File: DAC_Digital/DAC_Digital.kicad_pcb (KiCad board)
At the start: 2 copper layers, 100 x 100 mm, 131 parts, among them J1 +5V_in, J10 USB_Dev4, J11 P9, J12 Anlg_in, J13 Anlg_I2C, J14 P8, J15 Test, J16 Test, J17 Fix, J18 Fix, J19 Fix, J2 DBG_PORT, J20 Fix, J3 DSPL_PORT, J4 Out_SPDIF, J5 USB0, J6 USB1, J7 USB_Dev1, J8 USB_Dev2, J9 USB_Dev3, Q1 2n7002, Q2 2N7002, Q3 FDS4435, Q4 FDS4435, Q5 2N7002, Q6 2N7002, T1 DA103C, U1 CS8406_2, U2 PIC18F6722, U3 74LVC1G08GW, U4 PCM2903C, U5 74LVC1G08GW, U6 USB2514B-AEZC, U7 NE5532, X1 7A-24.000MAAJ-T, Y1 10MHz, Y2 12MHz

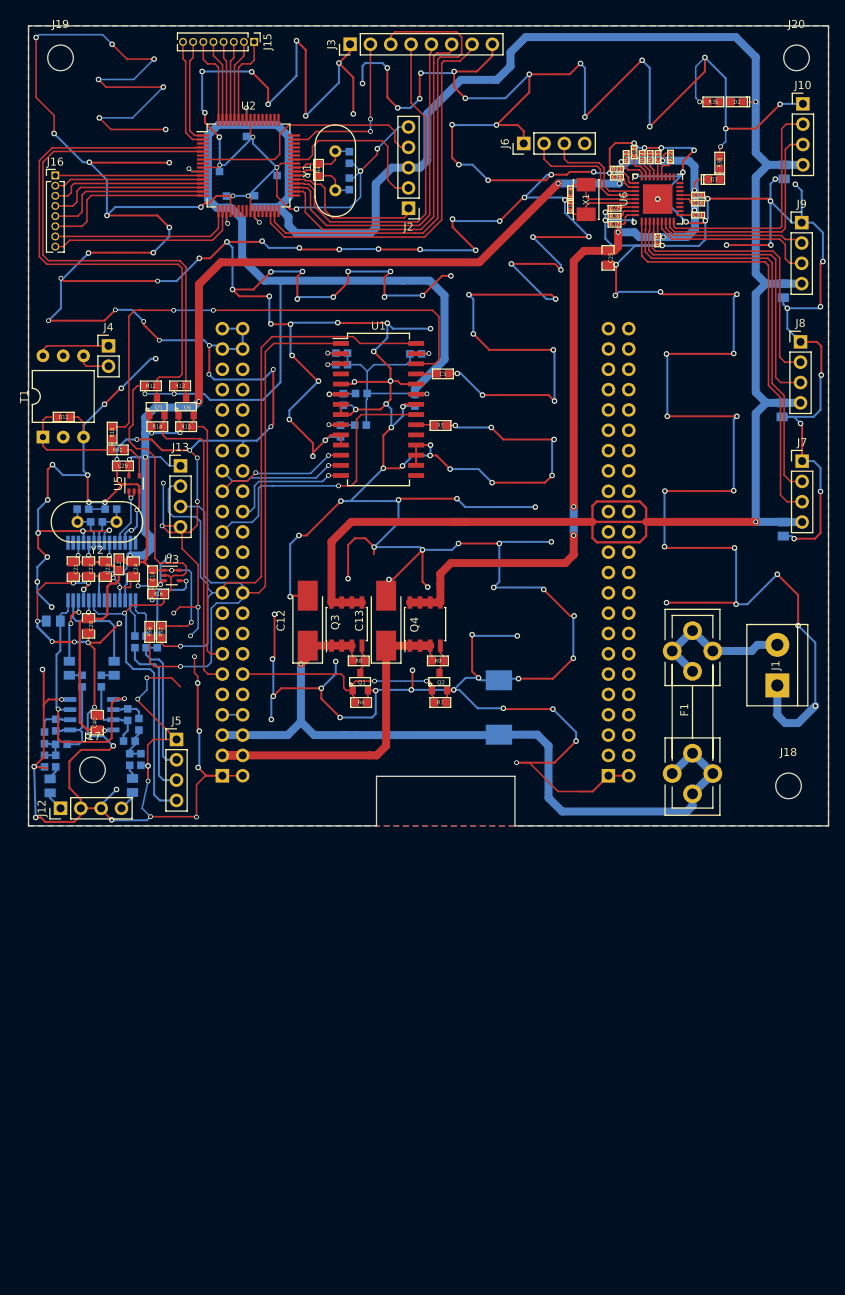
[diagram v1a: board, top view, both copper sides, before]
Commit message: Update DAC digital board, switch to odroid C2
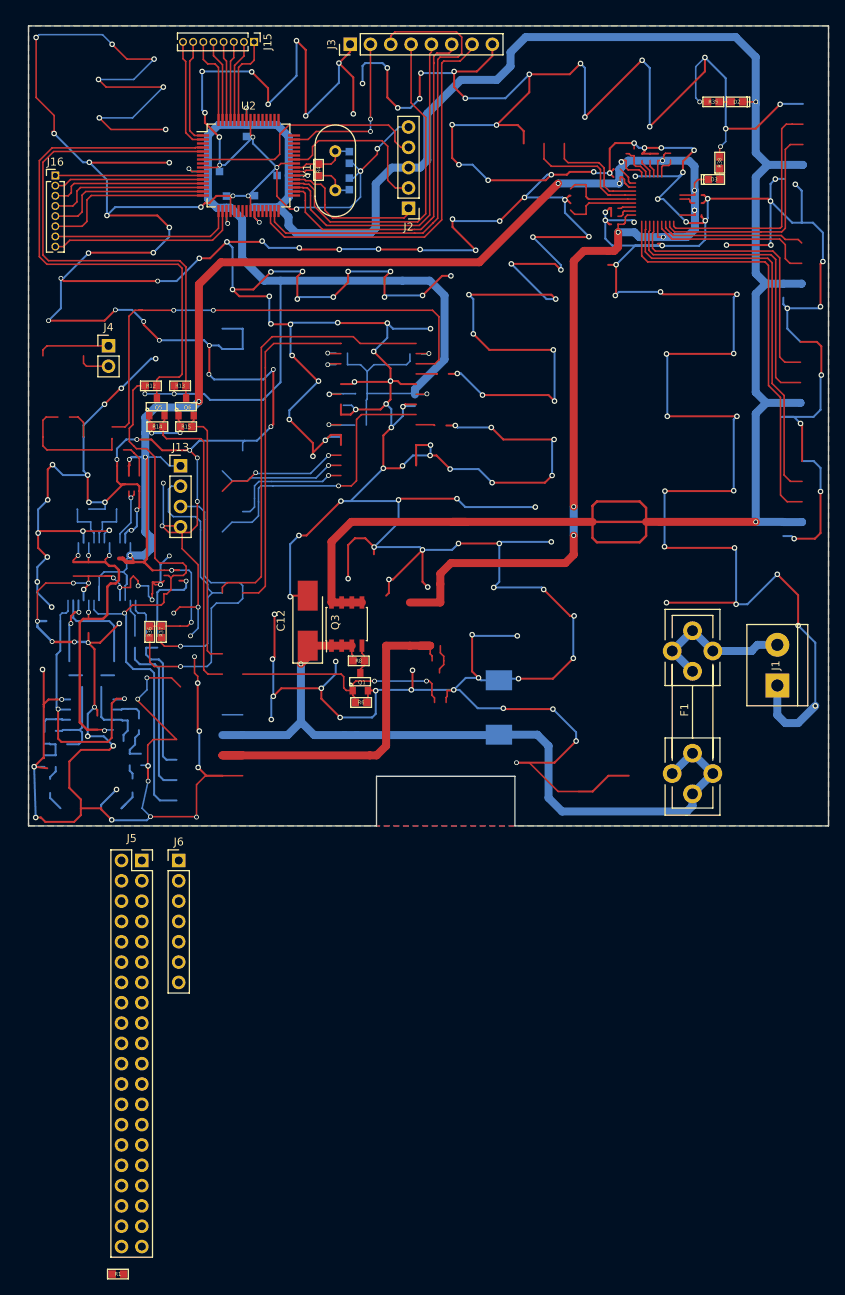
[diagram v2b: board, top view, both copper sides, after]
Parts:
- removed C1, C14, C2, C29, C3, C5: 100n, Yame_library:SM0603-MR
- removed C13: 100u, Capacitors_Tantalum_SMD:CP_Tantalum_Case-U_EIA-6032-15_Hand
- removed C15, C16: 18p, Yame_library:SM0603-MR
- removed C17, C19: 18p, Yame_library:SM0402-MR
- removed C18, C27, C28, C30, C31, C32, C35, C36, C37: 100n, Yame_library:SM0402-MR
- removed C20, C21, C22, C23, C24, C25, C26, C33, C34, C40, C43, C44, C45, C46, C47, C48: 10u, Yame_library:SM0805-MR
- removed C38, C39, C41, C42: 330p, Yame_library:SM0603-MR
- removed J10: USB_Dev4, Pin_Headers:Pin_Header_Straight_1x04_Pitch2.54mm
- removed J11: P9, Pin_Headers:Pin_Header_Straight_2x23_Pitch2.54mm
- removed J12: Anlg_in, Pin_Headers:Pin_Header_Straight_1x04_Pitch2.54mm
- removed J14: P8, Pin_Headers:Pin_Header_Straight_2x23_Pitch2.54mm
- removed J17, J18, J19, J20: Fix, Mounting_Holes:MountingHole_3.2mm_M3
- removed J7: USB_Dev1, Pin_Headers:Pin_Header_Straight_1x04_Pitch2.54mm
- removed J8: USB_Dev2, Pin_Headers:Pin_Header_Straight_1x04_Pitch2.54mm
- removed J9: USB_Dev3, Pin_Headers:Pin_Header_Straight_1x04_Pitch2.54mm
- removed L1, L2: BLM18AG102SN1D, Yame_library:SM0603-MR
- removed Q2: 2N7002, Yame_library:SOT23-MR
- removed Q4: FDS4435, Housings_SOIC:SOIC-8_3.9x4.9mm_Pitch1.27mm
- removed R10, R40: 390, Yame_library:SM0603-MR
- removed R11: 91, Yame_library:SM0603-MR
- removed R16, R17: 1M, Yame_library:SM0603-MR
- removed R18: 1,5k, Yame_library:SM0603-MR
- removed R19, R20: 22, Yame_library:SM0603-MR
- removed R2, R3: R, Yame_library:SM0603-MR
- removed R21, R22, R23, R24, R25: 47k, Yame_library:SM0402-MR
- removed R26: 12k, Yame_library:SM0402-MR
- removed R27, R28: 100, Yame_library:SM0603-MR
- removed R29, R30, R33, R34: 12k, Yame_library:SM0603-MR
- removed R31, R32: 3.9k, Yame_library:SM0603-MR
- removed R39, R7, R9: 1meg, Yame_library:SM0603-MR
- removed R5: 47k, Yame_library:SM0603-MR
- removed T1: DA103C, Housings_DIP:DIP-6_W10.16mm
- removed U1: CS8406_2, Housings_SOIC:SOIC-28W_7.5x18.7mm_Pitch1.27mm
- removed U3, U5: 74LVC1G08GW, TO_SOT_Packages_SMD:SOT-353_SC-70-5
- removed U4: PCM2903C, Housings_SSOP:SSOP-28_5.3x10.2mm_Pitch0.65mm
- removed U6: USB2514B-AEZC, Housings_DFN_QFN:QFN-36-1EP_6x6mm_Pitch0.5mm
- removed U7: NE5532, Housings_SOIC:SOIC-8_3.9x4.9mm_Pitch1.27mm
- removed X1: 7A-24.000MAAJ-T, Yame_library:7A_SERIES_TXC
- removed Y2: 12MHz, Crystals:Crystal_HC49-4H_Vertical
- J5: value USB0 -> Conn_02x20_Odd_Even; footprint Pin_Headers:Pin_Header_Straight_1x04_Pitch2.54mm -> Connector_PinSocket_2.54mm:PinSocket_2x20_P2.54mm_Vertical
- J6: value USB1 -> Conn_01x07; footprint Pin_Headers:Pin_Header_Straight_1x04_Pitch2.54mm -> Connector_PinHeader_2.54mm:PinHeader_1x07_P2.54mm_Vertical
- R1: value R -> 10k; moved to F.Cu
- moved R1 118.5 mm to (33.2, 244.0)
- moved J6 99.5 mm to (40.8, 192.3), turned to 0 degrees
- moved J5 15.7 mm to (36.2, 192.3)
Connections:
- net /VDD_5V_USB1 renamed Net-(J6-Pad4)
- net Net-(J3-Pad2) renamed /IntIR
- net Net-(J3-Pad3) renamed /IntB
- net Net-(J3-Pad4) renamed /MOSI
- net Net-(J3-Pad5) renamed /MISO
- net Net-(J3-Pad6) renamed /SCK
- net Net-(J3-Pad7) renamed //CS
- net VCC renamed /+3.3v_Dev
- C10 pad 2: GND -> GNDD
- C11 pad 2: GND -> GNDD
- C12 pad 2: GND -> GNDD
- C4 pad 2: GND -> GNDD
- C6 pad 2: GND -> GNDD
- C7 pad 2: GND -> GNDD
- C8 pad 2: GND -> GNDD
- C9 pad 2: GND -> GNDD
- D1 pad 2: GND -> GNDD
- J1 pad 1: GND -> GNDD
- J13 pad 4: GND -> GNDD
- J2 pad 3: /+5v_Dev -> /VDD_5V
- J2 pad 5: GND -> GNDD
- J3 pad 1: GND -> GNDD
- J3 pad 8: GND -> GNDD
- J5 pad 1: GND -> Net-(J5-Pad1)
- J5 pad 4: /+5v_Dev -> Net-(J5-Pad4)
- J6 pad 1: GND -> Net-(J6-Pad1)
- Q1 pad 2: GND -> GNDD
- R1 pad 1: Net-(R1-Pad1) -> /VDD_5V
- R1 pad 2: /+5v_Dev -> Net-(J2-Pad4)
- R12 pad 1: /+5v_Dev -> /VDD_5V
- R13 pad 1: /+5v_Dev -> /VDD_5V
- R35 pad 2: GND -> GNDD
- R38 pad 2: GND -> GNDD
- R6 pad 2: GND -> GNDD
- U2 pad 10: /+5v_Dev -> /VDD_5V
- U2 pad 19: /+5v_Dev -> /VDD_5V
- U2 pad 20: GND -> GNDD
- U2 pad 25: GND -> GNDD
- U2 pad 26: /+5v_Dev -> /VDD_5V
- U2 pad 38: /+5v_Dev -> /VDD_5V
- U2 pad 41: GND -> GNDD
- U2 pad 56: GND -> GNDD
- U2 pad 57: /+5v_Dev -> /VDD_5V
- U2 pad 9: GND -> GNDD
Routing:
- net GNDD: track 0.00 -> 1745.5 mm, vias 0 -> 266
- net GND: track 1745.5 -> 0.00 mm, vias 266 -> 0
- added copper zone on B.Cu, net GNDD
- added copper zone on F.Cu, net GNDD
- removed copper zone on B.Cu, net GND
- removed copper zone on F.Cu, net GND
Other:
- board text added: "1"
- board text added: "2"
- board text added: "23.5mm"
- board text added: "39"
- board text added: "40"
- board text added: "49.00mm"
- board text added: "56mm"
- board text added: "58mm"
- board text added: "5V DCJACK"
- board text added: "85mm"
- board text added: "ALIVE"
- board text added: "C10"
- board text added: "C100"
- board text added: "C101A"
- board text added: "C101B"
- board text added: "C102A"
- board text added: "C102B"
- board text added: "C103A"
- board text added: "C103B"
- board text added: "C104"
- board text added: "C105"
- board text added: "C106"
- board text added: "C107"
- board text added: "C108"
- board text added: "C109"
- board text added: "C11"
- board text added: "C112"
- board text added: "C113"
- board text added: "C114"
- board text added: "C12"
- board text added: "C124"
- board text added: "C136"
- board text added: "C14"
- board text added: "C15"
- board text added: "C159"
- board text added: "C160"
- board text added: "C164"
- board text added: "C22"
- board text added: "C23"
- board text added: "C25"
- board text added: "C27"
- board text added: "C28"
- board text added: "C29"
- board text added: "C3"
- board text added: "C30"
- board text added: "C38"
- board text added: "C4"
- board text added: "C40"
- board text added: "C42"
- board text added: "C43"
- board text added: "C44"
- board text added: "C45"
- board text added: "C46"
- board text added: "C48"
- board text added: "C52"
- board text added: "C57"
- board text added: "C58"
- board text added: "C59"
- board text added: "C6"
- board text added: "C60"
- board text added: "C61"
- board text added: "C62"
- board text added: "C63"
- board text added: "C64"
- board text added: "C65"
- board text added: "C66"
- board text added: "C67"
- board text added: "C68"
- board text added: "C69"
- board text added: "C7"
- board text added: "C71"
- board text added: "C72"
- board text added: "C75"
- board text added: "C76"
- board text added: "C77"
- board text added: "C78"
- board text added: "C79"
- board text added: "C8"
- board text added: "C82"
- board text added: "C83"
- board text added: "C84"
- board text added: "C86"
- board text added: "C87"
- board text added: "C88"
- board text added: "C89"
- board text added: "C90"
- board text added: "C91"
- board text added: "C92"
- board text added: "C95"
- board text added: "C96"
- board text added: "C97"
- board text added: "C98"
- board text added: "C99"
- board text added: "CON2"
- board text added: "CON3"
- board text added: "CON5"
- board text added: "CON6A"
- board text added: "CON6B"
- board text added: "CVBS"
- board text added: "D1"
- board text added: "D2"
- board text added: "FB1"
- board text added: "FB3"
- board text added: "GIGABIT Ethernet"
- board text added: "HARDKERNEL"
- board text added: "HDMI"
- board text added: "IR"
- board text added: "J1"
- board text added: "J2"
- board text added: "J3"
- board text added: "J4"
- board text added: "J6"
- board text added: "J7"
- board text added: "J8"
- board text added: "L10"
- board text added: "L3"
- board text added: "L4"
- board text added: "L5"
- board text added: "L6"
- board text added: "L7"
- board text added: "L8A"
- board text added: "L8B"
- board text added: "L9A"
- board text added: "L9B"
- board text added: "Micro"
- board text added: "ODROID-C2"
- board text added: "PWR"
- board text added: "Q1"
- board text added: "Q4"
- board text added: "Q5"
- board text added: "R106"
- board text added: "R107"
- board text added: "R109"
- board text added: "R111"
- board text added: "R112"
- board text added: "R113"
- board text added: "R12"
- board text added: "R13"
- board text added: "R14"
- board text added: "R15"
- board text added: "R16"
- board text added: "R17"
- board text added: "R18"
- board text added: "R19"
- board text added: "R23"
- board text added: "R24"
- board text added: "R25"
- board text added: "R26"
- board text added: "R27"
- board text added: "R28"
- board text added: "R29"
- board text added: "R30"
- board text added: "R31"
- board text added: "R32"
- board text added: "R33"
- board text added: "R34"
- board text added: "R35"
- board text added: "R37"
- board text added: "R38"
- board text added: "R4"
- board text added: "R40"
- board text added: "R42"
- board text added: "R43"
- board text added: "R44"
- board text added: "R45"
- board text added: "R46"
- board text added: "R5"
- board text added: "R52"
- board text added: "R53"
- board text added: "R56"
- board text added: "R57"
- board text added: "R59"
- board text added: "R61"
- board text added: "R62"
- board text added: "R63"
- board text added: "R64"
- board text added: "R65"
- board text added: "R66"
- board text added: "R67"
- board text added: "R68"
- board text added: "R69"
- board text added: "R74"
- board text added: "R75"
- board text added: "R76"
- board text added: "R77"
- board text added: "R78"
- board text added: "R79"
- board text added: "R80"
- board text added: "R81"
- board text added: "R84"
- board text added: "R85"
- board text added: "R86"
- board text added: "R87"
- board text added: "R88"
- board text added: "R89"
- board text added: "R90"
- board text added: "R91A"
- board text added: "R91B"
- board text added: "R92"
- board text added: "R93"
- board text added: "R94"
- board text added: "R95"
- board text added: "R96"
- board text added: "R97"
- board text added: "R98"
- board text added: "REV 0.2 20160226"
- board text added: "U1"
- board text added: "U10"
- board text added: "U11"
- board text added: "U14"
- board text added: "U15"
- board text added: "U17"
- board text added: "U18"
- board text added: "U19A"
- board text added: "U19B"
- board text added: "U20"
- board text added: "U21"
- board text added: "U3"
- board text added: "U5"
- board text added: "U7"
- board text added: "U8"
- board text added: "U9"
- board text added: "UART"
- board text added: "USB"
- board text added: "USB2.0 X 4"
- board text added: "X1"
- board text added: "X2"
- board text added: "X3"

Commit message: Update DAC_Digital sch
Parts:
- removed J15, J16: Test, Pin_Headers:Pin_Header_Straight_1x08_Pitch1.27mm
- added H1: MountingHole, MountingHole:MountingHole_3.2mm_M3_DIN965_Pad, F.Cu at (-0.42, -18.5)
- added H2: MountingHole, MountingHole:MountingHole_3.2mm_M3_DIN965_Pad, F.Cu at (4.23, -25.7)
- added H3: MountingHole, MountingHole:MountingHole_3.2mm_M3_DIN965_Pad, F.Cu at (11.4, -25.7)
- added H4: MountingHole, MountingHole:MountingHole_3.2mm_M3_DIN965_Pad, F.Cu at (6.73, -18.6)
- added J7: Conn_01x02, Connector_PinHeader_2.54mm:PinHeader_1x02_P2.54mm_Vertical, F.Cu at (-1.67, -27.0)
- C10, C11, C4, C6, C7, C8, C9, R1, R12, R13, R14, R15, R35, R36, R37, R38, R4, R6, R8: footprint Yame_library:SM0603-MR -> Resistor_SMD:R_0603_1608Metric
- D1: footprint Diodes_SMD:D_SMC -> Diode_SMD:D_SMC
- D2, D3: footprint Yame_library:SM0603-LED-MR -> LED_SMD:LED_0603_1608Metric
- F1: footprint Fuse_Holders_and_Fuses:Fuseholder5x20_horiz_open_universal_Type-III -> Yame_library:Fuse_5x20
- J1: footprint Connectors:bornier2 -> TerminalBlock:TerminalBlock_bornier-2_P5.08mm
- J13: footprint Pin_Headers:Pin_Header_Straight_1x04_Pitch2.54mm -> Connector_PinHeader_2.54mm:PinHeader_1x04_P2.54mm_Vertical
- J2: footprint Pin_Headers:Pin_Header_Straight_1x05_Pitch2.54mm -> Connector_PinHeader_2.54mm:PinHeader_1x05_P2.54mm_Horizontal
- J3: footprint Pin_Headers:Pin_Header_Straight_1x08_Pitch2.54mm -> Connector_PinHeader_2.54mm:PinHeader_1x08_P2.54mm_Horizontal
- J4: footprint Pin_Headers:Pin_Header_Straight_1x02_Pitch2.54mm -> Connector_PinHeader_2.54mm:PinHeader_1x02_P2.54mm_Vertical
- J6: footprint Connector_PinHeader_2.54mm:PinHeader_1x07_P2.54mm_Vertical -> Connector_PinSocket_2.54mm:PinSocket_1x07_P2.54mm_Vertical
- Q1, Q5, Q6: footprint Yame_library:SOT23-MR -> Package_TO_SOT_SMD:SOT-23
- Q3: footprint Housings_SOIC:SOIC-8_3.9x4.9mm_Pitch1.27mm -> Package_SO:SO-8_5.3x6.2mm_P1.27mm
- Y1: footprint Crystals:Crystal_HC49-4H_Vertical -> Crystal:Crystal_HC49-U_Vertical
- moved J2 39.4 mm to (35.7, 90.5), turned to 90 degrees
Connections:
- net /GPIO_60 renamed /Power_Dev
- net /I2C2_SCL renamed /SCL
- net /I2C2_SDA renamed /SDA
- net Net-(J5-Pad10) renamed /RXD1
- net Net-(J5-Pad11) renamed /GPIO_247
- net Net-(J5-Pad12) renamed /GPIO_238
- net Net-(J5-Pad13) renamed /GPIO_239
- net Net-(J5-Pad15) renamed /GPIO_237
- net Net-(J5-Pad16) renamed /GPIO_236
- net Net-(J5-Pad18) renamed /GPIO_233
- net Net-(J5-Pad19) renamed /PWM1
- net Net-(J5-Pad21) renamed /GPIO_232
- net Net-(J5-Pad22) renamed /GPIO_231
- net Net-(J5-Pad23) renamed /GPIO_230
- net Net-(J5-Pad24) renamed /GPIO_229
- net Net-(J5-Pad26) renamed /GPIO_225
- net Net-(J5-Pad27) renamed /I2CB_SDA
- net Net-(J5-Pad28) renamed /I2CB_SCL
- net Net-(J5-Pad29) renamed /GPIO_228
- net Net-(J5-Pad3) renamed /I2CA_SDA
- net Net-(J5-Pad31) renamed /GPIO_219
- net Net-(J5-Pad32) renamed /GPIO_224
- net Net-(J5-Pad33) renamed /PWM0
- net Net-(J5-Pad35) renamed /GPIO_214
- net Net-(J5-Pad36) renamed /GPIO_218
- net Net-(J5-Pad37) renamed /ADC.AIN1
- net Net-(J5-Pad38) renamed /1.8V
- net Net-(J5-Pad40) renamed /ADC.AIN0
- net Net-(J5-Pad5) renamed /I2CA_SCL
- net Net-(J5-Pad7) renamed /GPIO_249
- net Net-(J5-Pad8) renamed /TXD1
- net Net-(J6-Pad2) renamed /SPDIF
- net Net-(J6-Pad4) renamed /I2S_MCLK
- net Net-(J6-Pad5) renamed /I2S_LRCLK
- net Net-(J6-Pad6) renamed /I2S_SCLK
- net Net-(J6-Pad7) renamed /I2S_Data_Out
- J5 pad 1: Net-(J5-Pad1) -> /VDD_3V3B
- J5 pad 14: Net-(J5-Pad14) -> GNDD
- J5 pad 17: Net-(J5-Pad17) -> /VDD_3V3B
- J5 pad 2: Net-(J5-Pad2) -> /VDD_5V
- J5 pad 20: Net-(J5-Pad20) -> GNDD
- J5 pad 25: Net-(J5-Pad25) -> GNDD
- J5 pad 30: Net-(J5-Pad30) -> GNDD
- J5 pad 34: Net-(J5-Pad34) -> GNDD
- J5 pad 39: Net-(J5-Pad39) -> GNDD
- J5 pad 4: Net-(J5-Pad4) -> /VDD_5V
- J5 pad 6: Net-(J5-Pad6) -> GNDD
- J5 pad 9: Net-(J5-Pad9) -> GNDD
- J6 pad 1: Net-(J6-Pad1) -> GNDD
- J6 pad 3: Net-(J6-Pad3) -> /VDD_5V
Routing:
- net /SCL: track 88.2 -> 33.1 mm
- net /I2C2_SCL: track 0.00 -> 55.0 mm
- net /SDA: track 82.9 -> 40.6 mm
- net /I2C2_SDA: track 0.00 -> 42.4 mm
- net /Power_Dev: track 30.5 -> 0.00 mm, vias 2 -> 0
- net /GPIO_60: track 0.00 -> 30.5 mm, vias 0 -> 2
- net Net-(J5-Pad3): track 0.00 -> 20.8 mm
- net /I2CA_SDA: track 20.8 -> 0.00 mm
- net Net-(J6-Pad2): track 0.00 -> 16.6 mm
- net /SPDIF: track 16.6 -> 0.00 mm

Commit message: Update DAC_Digital component placement
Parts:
- added H5: MountingHole, MountingHole:MountingHole_3.2mm_M3_DIN965, F.Cu at (100.0, 168.0)
- added H6: MountingHole, MountingHole:MountingHole_3.2mm_M3_DIN965, F.Cu at (51.0, 168.0)
- added H7: MountingHole, MountingHole:MountingHole_3.2mm_M3_DIN965, F.Cu at (51.0, 110.0)
- added H8: MountingHole, MountingHole:MountingHole_3.2mm_M3_DIN965, F.Cu at (100.0, 110.0)
- added J8: Conn_01x02, Connector_PinHeader_2.54mm:PinHeader_1x02_P2.54mm_Vertical, F.Cu at (53.8, 90.3)
- F1, J5: moved to B.Cu
- moved H4 229.8 mm to (117.0, 183.0)
- moved H1 201.8 mm to (30.0, 181.0)
- moved J7 184.5 mm to (51.2, 149.8), turned to 270 degrees
- moved H2 163.7 mm to (118.0, 92.0)
- moved R1 147.6 mm to (38.5, 96.5)
- moved H3 118.6 mm to (26.0, 92.0)
- moved J5 99.5 mm to (98.7, 114.9), turned to 180 degrees
- moved R14 83.0 mm to (115.0, 106.9)
- moved Q5 83.0 mm to (115.0, 104.4)
- moved R12 83.0 mm to (114.2, 101.8)
- moved Q6 75.5 mm to (110.5, 104.4)
- moved R13 75.5 mm to (109.7, 101.8)
- moved R15 75.5 mm to (110.5, 106.9)
- moved D2 63.2 mm to (109.2, 160.7)
- moved R35 63.2 mm to (106.2, 160.7)
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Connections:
- J13 pad 2: /SCL -> /I2CA_SCL
- J13 pad 3: /SDA -> /I2CA_SDA
- J4 pad 1: Net-(J4-Pad1) -> /SPDIF
- J4 pad 2: Net-(J4-Pad2) -> GNDD
- Q1 pad 1: /Power_Dev -> /GPIO_249
- Q5 pad 2: /UART4_RXD -> /RXD1
- Q6 pad 2: /UART4_TXD -> /TXD1
- R1 pad 1: /VDD_5V -> /+5v_Dev
- R12 pad 1: /VDD_5V -> /+5v_Dev
- R13 pad 1: /VDD_5V -> /+5v_Dev
- R14 pad 2: /UART4_RXD -> /RXD1
- R15 pad 2: /UART4_TXD -> /TXD1
- R36 pad 2: /SDA -> /I2CA_SDA
- R37 pad 2: /SCL -> /I2CA_SCL
- R6 pad 1: /Power_Dev -> /GPIO_249
- U2 pad 10: /VDD_5V -> /+5v_Dev
- U2 pad 19: /VDD_5V -> /+5v_Dev
- U2 pad 26: /VDD_5V -> /+5v_Dev
- U2 pad 38: /VDD_5V -> /+5v_Dev
- U2 pad 57: /VDD_5V -> /+5v_Dev
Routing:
- net GNDD: track 1745.5 -> 0.00 mm, vias 266 -> 0
- net /+5v_Dev: track 492.0 -> 0.00 mm, vias 11 -> 0
- net /+3.3v_Dev: track 302.2 -> 0.00 mm, vias 18 -> 0
- net /VDD_5V: track 97.9 -> 0.00 mm, vias 1 -> 0
- net Net-(Q5-Pad3): track 70.6 -> 0.00 mm
- net Net-(Q6-Pad3): track 67.0 -> 0.00 mm
- net Net-(R10-Pad2): track 63.9 -> 0.00 mm, vias 2 -> 0
- net /IntB: track 58.7 -> 0.00 mm
- net /I2C2_SCL: track 55.0 -> 0.00 mm
- net /D-_Dev1: track 53.0 -> 0.00 mm
- net /D+_Dev1: track 50.0 -> 0.00 mm
- net //CS: track 49.2 -> 0.00 mm
- net /SCK: track 45.0 -> 0.00 mm
- net /VDD_3V3B: track 44.8 -> 0.00 mm
- net /Vanlg: track 43.8 -> 0.00 mm, vias 5 -> 0
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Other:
- outline, holes or cut-outs redrawn
- board text removed: "1"
- board text removed: "2"
- board text removed: "23.5mm"
- board text removed: "39"
- board text removed: "40"
- board text removed: "49.00mm"
- board text removed: "56mm"
- board text removed: "58mm"
- board text removed: "5V DCJACK"
- board text removed: "85mm"
- board text removed: "ALIVE"
- board text removed: "C10"
- board text removed: "C100"
- board text removed: "C101A"
- board text removed: "C101B"
- board text removed: "C102A"
- board text removed: "C102B"
- board text removed: "C103A"
- board text removed: "C103B"
- board text removed: "C104"
- board text removed: "C105"
- board text removed: "C106"
- board text removed: "C107"
- board text removed: "C108"
- board text removed: "C109"
- board text removed: "C11"
- board text removed: "C112"
- board text removed: "C113"
- board text removed: "C114"
- board text removed: "C12"
- board text removed: "C124"
- board text removed: "C136"
- board text removed: "C14"
- board text removed: "C15"
- board text removed: "C159"
- board text removed: "C160"
- board text removed: "C164"
- board text removed: "C22"
- board text removed: "C23"
- board text removed: "C25"
- board text removed: "C27"
- board text removed: "C28"
- board text removed: "C29"
- board text removed: "C3"
- board text removed: "C30"
- board text removed: "C38"
- board text removed: "C4"
- board text removed: "C40"
- board text removed: "C42"
- board text removed: "C43"
- board text removed: "C44"
- board text removed: "C45"
- board text removed: "C46"
- board text removed: "C48"
- board text removed: "C52"
- board text removed: "C57"
- board text removed: "C58"
- board text removed: "C59"
- board text removed: "C6"
- board text removed: "C60"
- board text removed: "C61"
- board text removed: "C62"
- board text removed: "C63"
- board text removed: "C64"
- board text removed: "C65"
- board text removed: "C66"
- board text removed: "C67"
- board text removed: "C68"
- board text removed: "C69"
- board text removed: "C7"
- board text removed: "C71"
- board text removed: "C72"
- board text removed: "C75"
- board text removed: "C76"
- board text removed: "C77"
- board text removed: "C78"
- board text removed: "C79"
- board text removed: "C8"
- board text removed: "C82"
- board text removed: "C83"
- board text removed: "C84"
- board text removed: "C86"
- board text removed: "C87"
- board text removed: "C88"
- board text removed: "C89"
- board text removed: "C90"
- board text removed: "C91"
- board text removed: "C92"
- board text removed: "C95"
- board text removed: "C96"
- board text removed: "C97"
- board text removed: "C98"
- board text removed: "C99"
- board text removed: "CON2"
- board text removed: "CON3"
- board text removed: "CON5"
- board text removed: "CON6A"
- board text removed: "CON6B"
- board text removed: "CVBS"
- board text removed: "D1"
- board text removed: "D2"
- board text removed: "FB1"
- board text removed: "FB3"
- board text removed: "GIGABIT Ethernet"
- board text removed: "HARDKERNEL"
- board text removed: "HDMI"
- board text removed: "IR"
- board text removed: "J1"
- board text removed: "J2"
- board text removed: "J3"
- board text removed: "J4"
- board text removed: "J6"
- board text removed: "J7"
- board text removed: "J8"
- board text removed: "L10"
- board text removed: "L3"
- board text removed: "L4"
- board text removed: "L5"
- board text removed: "L6"
- board text removed: "L7"
- board text removed: "L8A"
- board text removed: "L8B"
- board text removed: "L9A"
- board text removed: "L9B"
- board text removed: "Micro"
- board text removed: "ODROID-C2"
- board text removed: "PWR"
- board text removed: "Q1"
- board text removed: "Q4"
- board text removed: "Q5"
- board text removed: "R106"
- board text removed: "R107"
- board text removed: "R109"
- board text removed: "R111"
- board text removed: "R112"
- board text removed: "R113"
- board text removed: "R12"
- board text removed: "R13"
- board text removed: "R14"
- board text removed: "R15"
- board text removed: "R16"
- board text removed: "R17"
- board text removed: "R18"
- board text removed: "R19"
- board text removed: "R23"
- board text removed: "R24"
- board text removed: "R25"
- board text removed: "R26"
- board text removed: "R27"
- board text removed: "R28"
- board text removed: "R29"
- board text removed: "R30"
- board text removed: "R31"
- board text removed: "R32"
- board text removed: "R33"
- board text removed: "R34"
- board text removed: "R35"
- board text removed: "R37"
- board text removed: "R38"
- board text removed: "R4"
- board text removed: "R40"
- board text removed: "R42"
- board text removed: "R43"
- board text removed: "R44"
- board text removed: "R45"
- board text removed: "R46"
- board text removed: "R5"
- board text removed: "R52"
- board text removed: "R53"
- board text removed: "R56"
- board text removed: "R57"
- board text removed: "R59"
- board text removed: "R61"
- board text removed: "R62"
- board text removed: "R63"
- board text removed: "R64"
- board text removed: "R65"
- board text removed: "R66"
- board text removed: "R67"
- board text removed: "R68"
- board text removed: "R69"
- board text removed: "R74"
- board text removed: "R75"
- board text removed: "R76"
- board text removed: "R77"
- board text removed: "R78"
- board text removed: "R79"
- board text removed: "R80"
- board text removed: "R81"
- board text removed: "R84"
- board text removed: "R85"
- board text removed: "R86"
- board text removed: "R87"
- board text removed: "R88"
- board text removed: "R89"
- board text removed: "R90"
- board text removed: "R91A"
- board text removed: "R91B"
- board text removed: "R92"
- board text removed: "R93"
- board text removed: "R94"
- board text removed: "R95"
- board text removed: "R96"
- board text removed: "R97"
- board text removed: "R98"
- board text removed: "REV 0.2 20160226"
- board text removed: "U1"
- board text removed: "U10"
- board text removed: "U11"
- board text removed: "U14"
- board text removed: "U15"
- board text removed: "U17"
- board text removed: "U18"
- board text removed: "U19A"
- board text removed: "U19B"
- board text removed: "U20"
- board text removed: "U21"
- board text removed: "U3"
- board text removed: "U5"
- board text removed: "U7"
- board text removed: "U8"
- board text removed: "U9"
- board text removed: "UART"
- board text removed: "USB"
- board text removed: "USB2.0 X 4"
- board text removed: "X1"
- board text removed: "X2"
- board text removed: "X3"

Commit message: Update layout
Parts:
- J6, J7: moved to B.Cu
- moved R35 65.3 mm to (118.6, 96.5)
- moved D2 62.9 mm to (118.6, 98.5), turned to 180 degrees
- moved D3 62.1 mm to (118.6, 109.5)
- moved R38 57.9 mm to (118.6, 111.5), turned to 180 degrees
- moved Y1 22.8 mm to (41.5, 98.7), turned to 180 degrees
- moved C8 19.7 mm to (43.4, 116.0), turned to 180 degrees
- moved R36 19.4 mm to (35.5, 144.4)
- moved R37 19.4 mm to (37.5, 144.4)
- moved C7 18.4 mm to (39.5, 117.5), turned to 90 degrees
- moved C4 18.4 mm to (40.7, 100.8), turned to 180 degrees
- moved C6 16.3 mm to (37.4, 100.8), turned to 0 degrees
- moved C9 15.5 mm to (43.3, 112.5), turned to 180 degrees
- moved J1 15.0 mm to (109.2, 184.1)
- moved R4 11.0 mm to (39.3, 104.2), turned to 0 degrees
- moved C11 9.90 mm to (34.5, 113.5), turned to 0 degrees
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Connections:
- J2 pad 3: /VDD_5V -> /+5v_Dev
- J5 pad 1: /VDD_3V3B -> /+3.3v_Dev
- J5 pad 2: /VDD_5V -> /C2_5V
- J5 pad 4: /VDD_5V -> /C2_5V
- J6 pad 3: /VDD_5V -> /C2_2_5V
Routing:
- net /+5v_Dev: track 0.00 -> 182.2 mm, vias 0 -> 9
- net /VDD_5V: track 0.00 -> 158.6 mm
- net /+3.3v_Dev: track 0.00 -> 129.5 mm
- net Net-(Q5-Pad3): track 0.00 -> 98.0 mm
- net /I2CA_SDA: track 0.00 -> 93.3 mm
- net Net-(Q6-Pad3): track 0.00 -> 92.5 mm
- net /I2CA_SCL: track 0.00 -> 83.2 mm
- net Net-(J2-Pad4): track 0.00 -> 69.8 mm, vias 0 -> 1
- net /IntIR: track 0.00 -> 57.3 mm
- net //CS: track 0.00 -> 56.0 mm
- net /SCK: track 0.00 -> 47.9 mm
- net /MISO: track 0.00 -> 46.1 mm
- net /IntB: track 0.00 -> 45.3 mm, vias 0 -> 1
- net /MOSI: track 0.00 -> 44.1 mm
- net /SPDIF: track 0.00 -> 31.6 mm
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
